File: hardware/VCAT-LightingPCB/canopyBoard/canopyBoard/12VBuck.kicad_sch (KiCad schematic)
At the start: 0 parts

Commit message: please no overrides, complete with bus, hopefully
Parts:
- added C10: 100n, Capacitor_SMD:C_0603_1608Metric, symbol Device:C_Small
- added C11, C12: 22u, Capacitor_SMD:C_1210_3225Metric_Pad1.33x2.70mm_HandSolder, symbol Device:C
- added C13: 3.3u, Capacitor_SMD:C_0805_2012Metric_Pad1.18x1.45mm_HandSolder, symbol Device:C
- added C8: 4.7u, Capacitor_SMD:C_0805_2012Metric_Pad1.18x1.45mm_HandSolder, symbol Device:C_Small
- added C9: 100n, Capacitor_SMD:C_0603_1608Metric_Pad1.08x0.95mm_HandSolder, symbol Device:C_Small
- added L1: 8.2u, LHRS_Passives:74439369082, symbol Device:L_Small
- added R7: 100k, Resistor_SMD:R_0603_1608Metric, symbol Device:R_Small
- added R8: 19.1k, Resistor_SMD:R_0603_1608Metric, symbol Device:R_Small
- added TP1: V_in_12V, TestPoint:TestPoint_THTPad_D3.0mm_Drill1.5mm, symbol Connector:TestPoint
- added TP2: CB, TestPoint:TestPoint_THTPad_D3.0mm_Drill1.5mm, symbol Connector:TestPoint
- added TP3: FB, TestPoint:TestPoint_THTPad_D3.0mm_Drill1.5mm, symbol Connector:TestPoint
- added TP4: SW, TestPoint:TestPoint_THTPad_D3.0mm_Drill1.5mm, symbol Connector:TestPoint
- added U1: LMR51635XDDCR, DDC0006A-MFG, symbol lhrs_power:LMR51635XDDCR
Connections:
- new net CB: C10.1, TP2.1, U1.6 (CB)
- new net FB: R7.2, R8.1, TP3.1, U1.1 (FB)
- new net GND: C11.2, C12.2, C13.2, C8.2, C9.2, R8.2, U1.4 (GND)
- new net SW: C10.2, L1.1, TP4.1, U1.5 (SW)
- new net V_in_12V: C8.1, C9.1, TP1.1, U1.2 (EN), U1.3 (VIN)
- new net V_out_5V: C11.1, C12.1, C13.1, L1.2, R7.1
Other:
- note added: "12V Vout"
- note added: "12V-5V Buck Converter"
- note added: "Fsw 400khz"
- note added: "Test Points"
- note added: "Vout 5"

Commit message: pray for no errors, more stuff to add
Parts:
- renumbered C8 to C1, C9 to C2, C10 to C3, C11 to C4, C12 to C5, C13 to C6, R7 to R1, R8 to R2

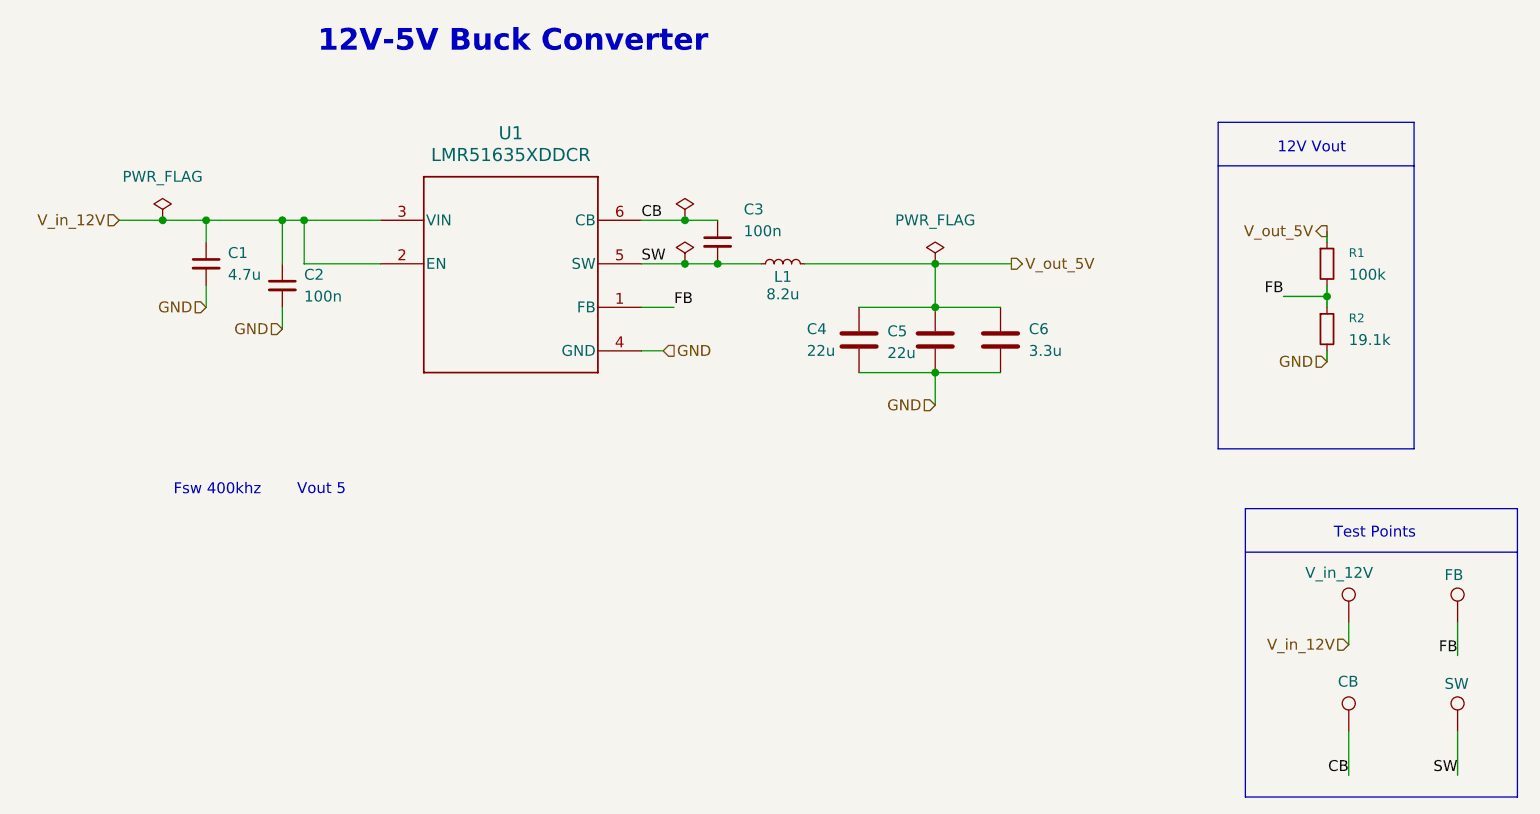
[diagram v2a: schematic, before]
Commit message: Untrack KiCad .history, convert KiCAD-Sharepoint to a submodule, remove LightsPCB
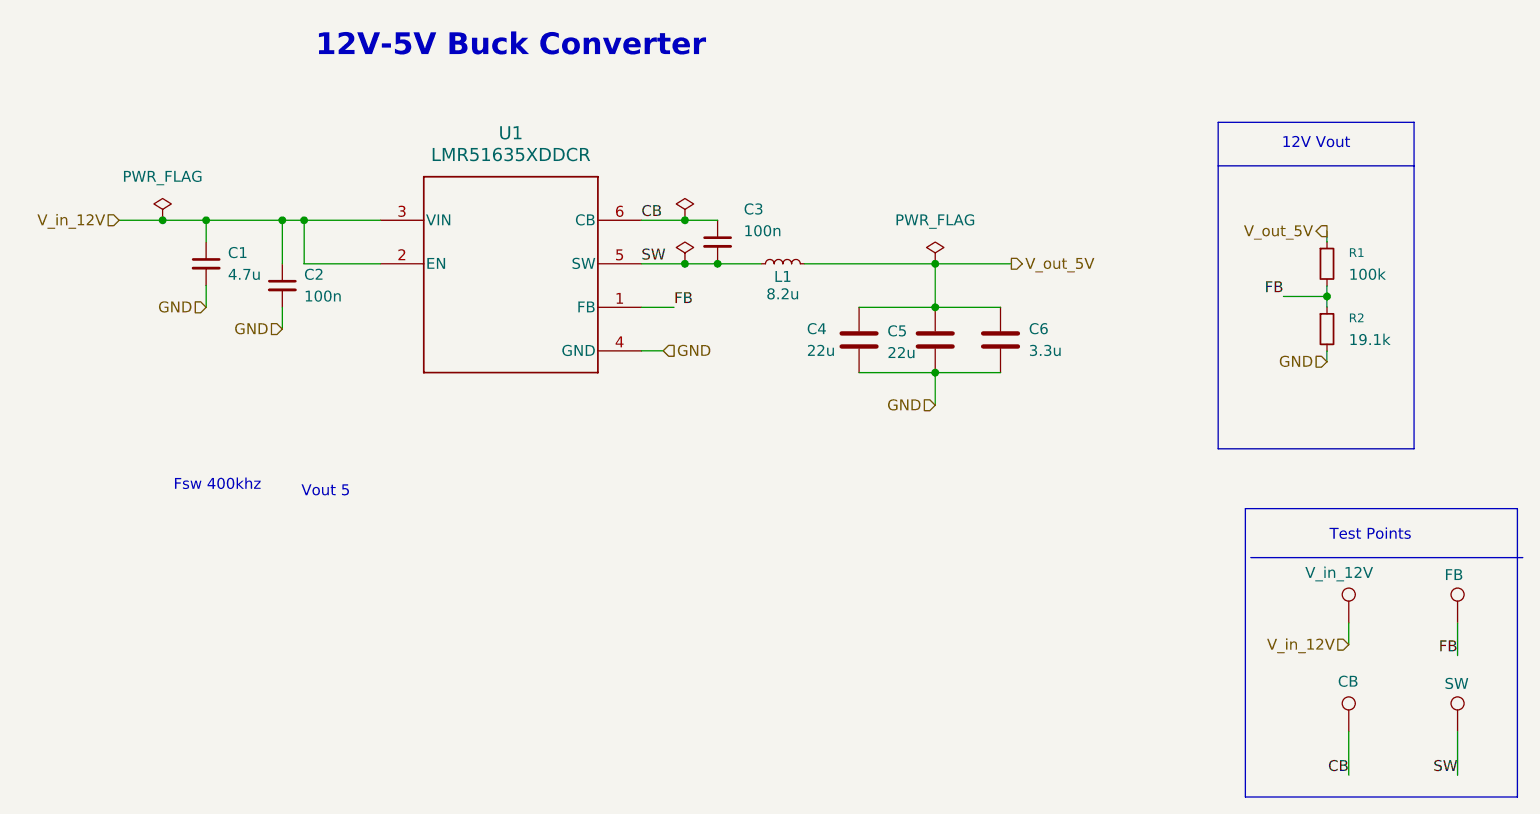
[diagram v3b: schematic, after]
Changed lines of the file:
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@@
 	(text "12V Vout"
 		(exclude_from_sim no)
-		(at 223.012 72.898 0)
+		(at 223.52 72.39 0)
 		(effects
 			(font
@@
 	(text "Test Points\n"
 		(exclude_from_sim no)
-		(at 230.378 117.856 0)
+		(at 229.87 118.11 0)
 		(effects
 			(font
@@
 	(text "Fsw 400khz"
 		(exclude_from_sim no)
-		(at 90.17 113.538 0)
+		(at 90.17 113.03 0)
 		(effects
 			(font
@@
 	(text "Vout 5"
 		(exclude_from_sim no)
-		(at 107.442 112.776 0)
+		(at 107.95 113.03 0)
 		(effects
 			(font
@@
 	(text "12V-5V Buck Converter"
 		(exclude_from_sim no)
-		(at 129.794 60.452 0)
+		(at 129.54 60.96 0)
 		(effects
 			(font
@@
 	(polyline
 		(pts
-			(xy 215.265 120.015) (xy 247.015 120.015)
+			(xy 215.9 120.65) (xy 247.65 120.65)
 		)
 		(stroke
